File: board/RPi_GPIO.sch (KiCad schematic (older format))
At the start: 35 parts, among them IC1 ATMEGA328-A, IC2 RFM69HW, J1 RPi_GPIO, P1 FTDI_CONN_01X06, P10 SW_CONN, P11 BATT_IN, P12 CONN_01X01, P2 D4, P3 ADC0, P4 ADC1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

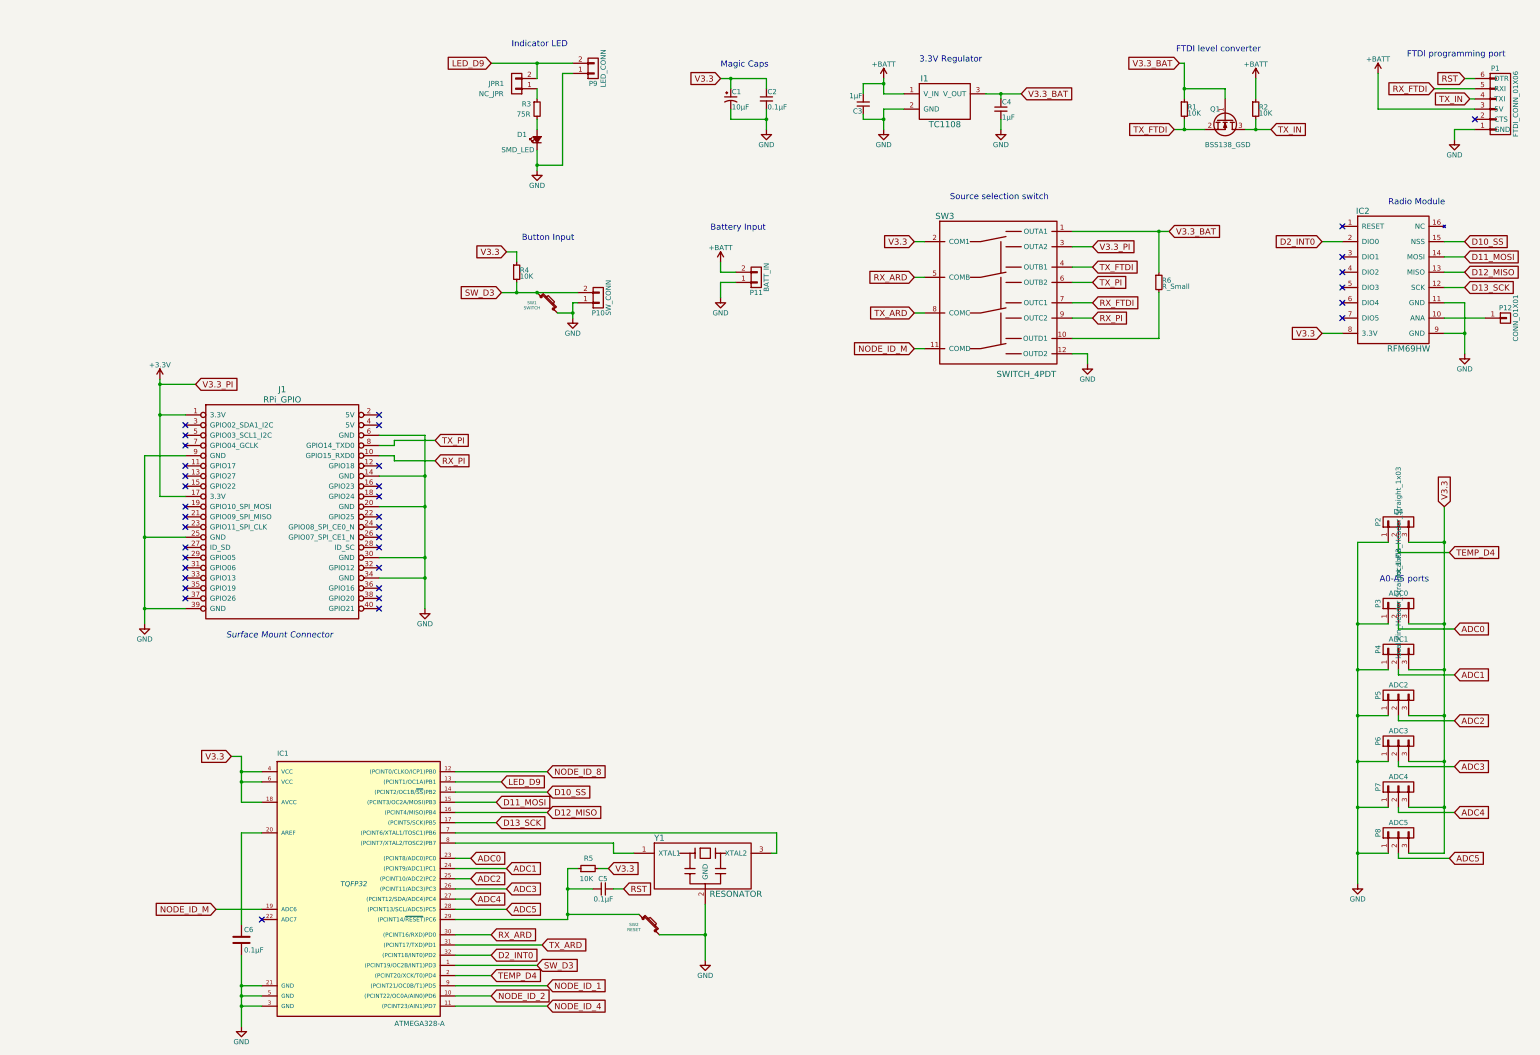
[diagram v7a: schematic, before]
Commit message: added node ID selection 4-way DIP switches
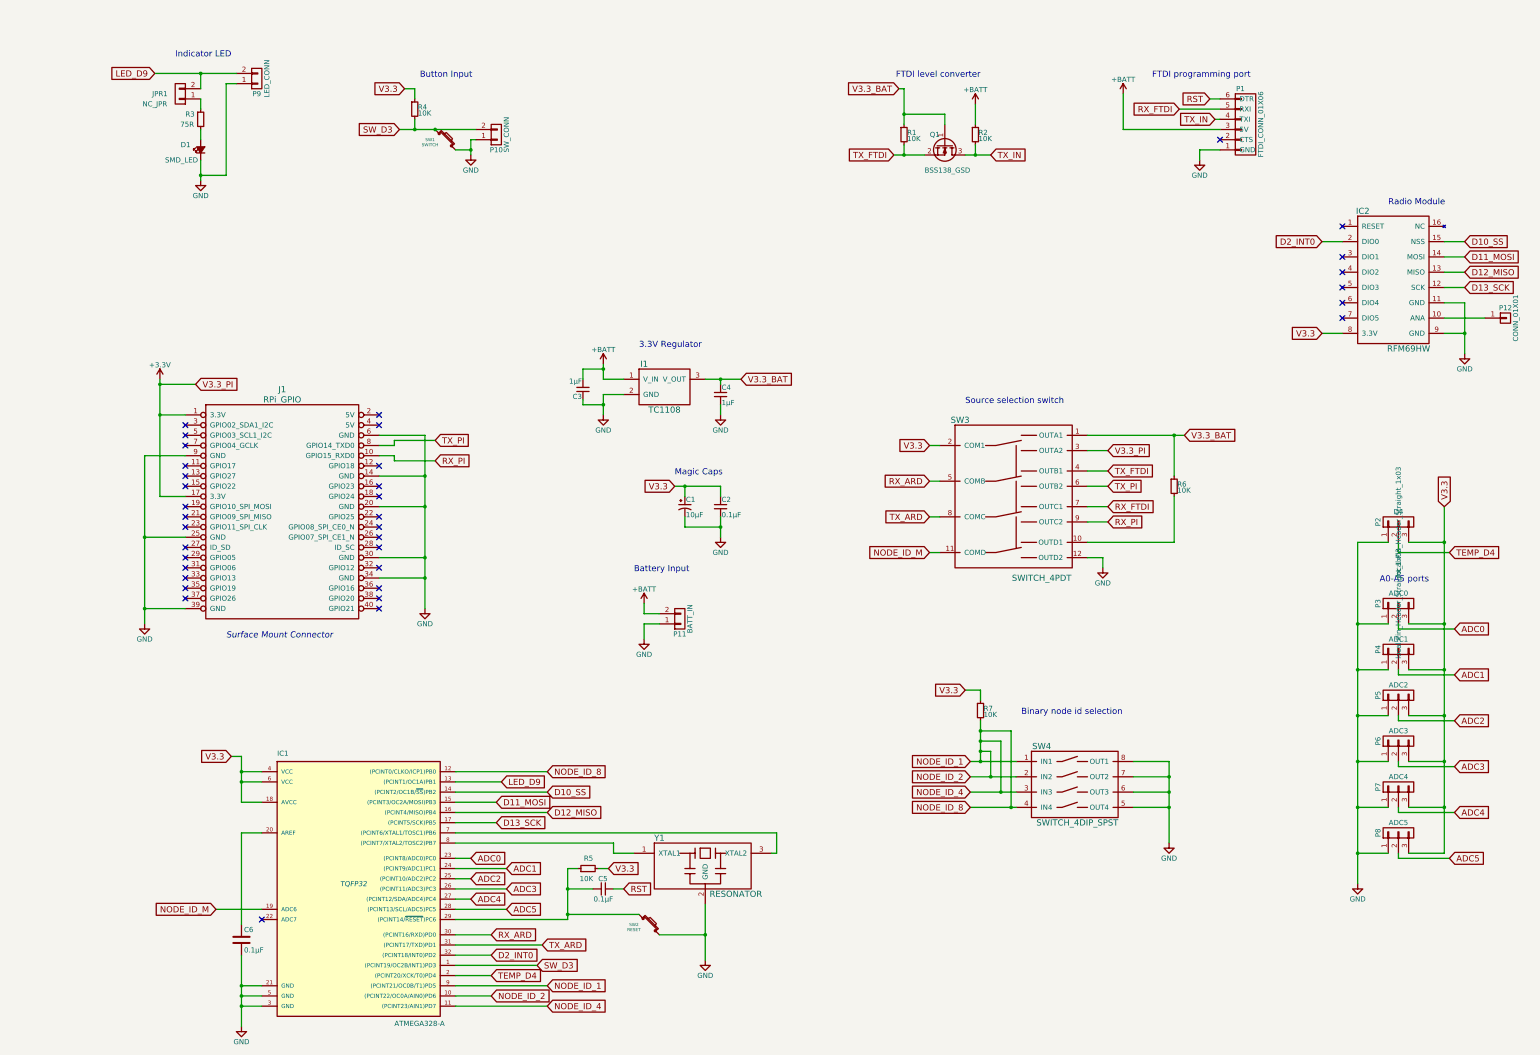
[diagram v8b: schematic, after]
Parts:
- added R7: 10K, symbol R_Small
- added SW4: SWITCH_4DIP_SPST, symbol SWITCH_4DIP_SPST
- R6: value R_Small -> 10K
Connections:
- net NODE_ID_2 is gone; now on net NODE_ID_1: IC1.10 ((PCINT22/OC0A/AIN0)PD6)
- net NODE_ID_4 is gone; now on net NODE_ID_1: IC1.11 ((PCINT23/AIN1)PD7)
- net NODE_ID_8 is gone; now on net NODE_ID_1: IC1.12 ((PCINT0/CLKO/ICP1)PB0)
- net GND: now also SW4.5 (OUT4), SW4.6 (OUT3), SW4.7 (OUT2), SW4.8 (OUT1)
- net NODE_ID_1: now also R7.2, SW4.1 (IN1), SW4.2 (IN2), SW4.3 (IN3), SW4.4 (IN4)
- net V3.3: now also R7.1
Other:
- note added: "Binary node id selection"
- moved on the sheet: C1, C2, C3, C4, D1, I1, JPR1, P1, P10, P11, P9, Q1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
